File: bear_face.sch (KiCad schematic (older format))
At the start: 275 parts, among them J1 USB_B_Micro, SW1 SW_Push, U1 ATmega32U4-AU, Y1 16MHz

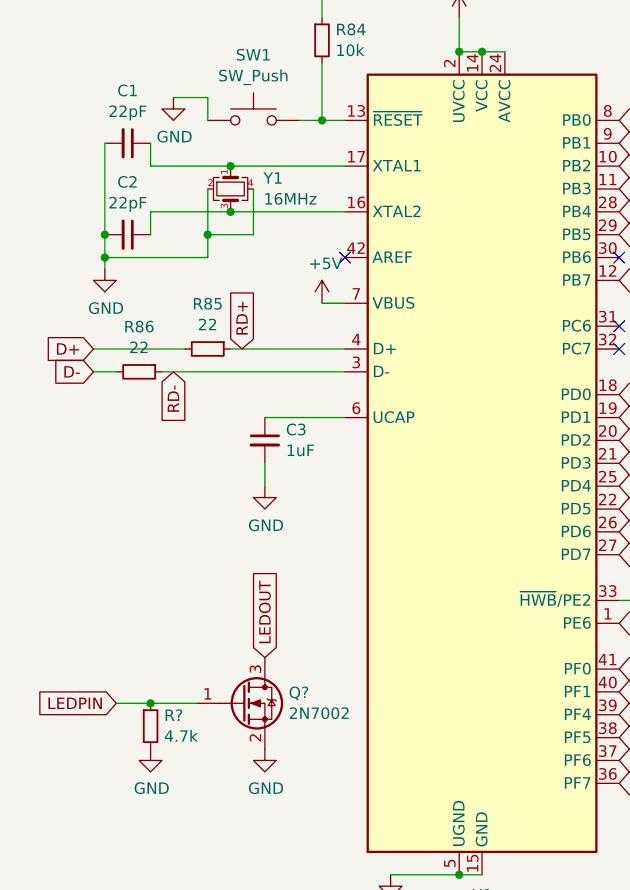
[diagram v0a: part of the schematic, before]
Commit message: Changed MCU components back to SMD
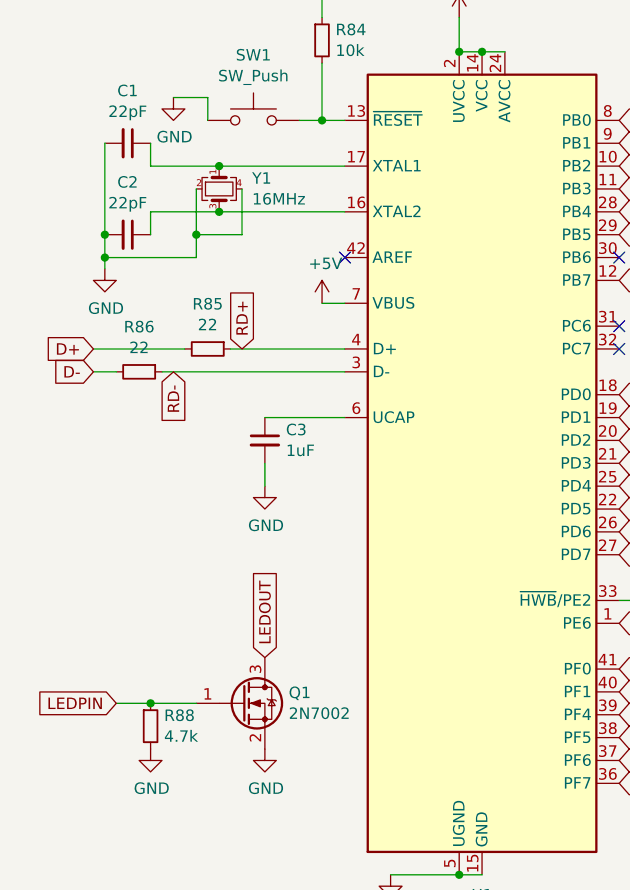
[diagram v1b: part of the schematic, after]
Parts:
- R85, R86: footprint Resistor_SMD:R_0805_2012Metric -> bear_face_parts:Resistor-THT
- R88: renamed from R?; footprint (none) -> bear_face_parts:Resistor-THT
- gave numbers to parts that had none: 1
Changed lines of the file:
@@
 F 0 "R85" V 1004 4800 50  0000 C CNN
 F 1 "22" V 1095 4800 50  0000 C CNN
-F 2 "Resistor_SMD:R_0805_2012Metric" H 1200 4800 50  0001 C CNN
+F 2 "bear_face_parts:Resistor-THT" H 1200 4800 50  0001 C CNN
 F 3 "~" H 1200 4800 50  0001 C CNN
 	1    1200 4800
@@
 F 0 "R86" V 704 4900 50  0000 C CNN
 F 1 "22" V 795 4900 50  0000 C CNN
-F 2 "Resistor_SMD:R_0805_2012Metric" H 900 4900 50  0001 C CNN
+F 2 "bear_face_parts:Resistor-THT" H 900 4900 50  0001 C CNN
 F 3 "~" H 900 4900 50  0001 C CNN
 	1    900  4900
@@
 	750  3900 750  4300
 Connection ~ 750  4300
-Wire Wire Line
-	750  4300 750  4400
 $Comp
 L power:GND #PWR08
@@
 Text GLabel 10950 4950 2    50   Input ~ 0
 ROW5
-Wire Wire Line
-	950  4000 1300 4000
-Wire Wire Line
-	950  4200 1300 4200
-$Comp
-L Device:Crystal_GND24_Small Y1
-U 1 1 5EE4C65A
-P 1300 4100
-F 0 "Y1" V 1254 4244 50  0000 L CNN
-F 1 "16MHz" V 1345 4244 50  0000 L CNN
-F 2 "Crystal:Crystal_SMD_3225-4Pin_3.2x2.5mm" H 1300 4100 50  0001 C CNN
-F 3 "~" H 1300 4100 50  0001 C CNN
-	1    1300 4100
-	0    1    1    0
-$EndComp
-Connection ~ 1300 4000
-Wire Wire Line
-	1300 4000 1800 4000
-Connection ~ 1300 4200
-Wire Wire Line
-	1300 4200 1800 4200
-Wire Wire Line
-	1200 4100 1200 4300
-Wire Wire Line
-	750  4400 1200 4400
-Connection ~ 750  4400
-Wire Wire Line
-	750  4400 750  4450
-Wire Wire Line
-	1400 4100 1400 4300
-Wire Wire Line
-	1400 4300 1200 4300
-Connection ~ 1200 4300
-Wire Wire Line
-	1200 4300 1200 4400
 Text GLabel 800  6350 0    50   Input ~ 0
 LEDPIN
 $Comp
-L Transistor_FET:2N7002 Q?
+L Transistor_FET:2N7002 Q1
 U 1 1 5E2E1EE1
 P 1350 6350
-F 0 "Q?" H 1554 6396 50  0000 L CNN
+F 0 "Q1" H 1554 6396 50  0000 L CNN
 F 1 "2N7002" H 1554 6305 50  0000 L CNN
 F 2 "Package_TO_SOT_SMD:SOT-23" H 1550 6275 50  0001 L CIN
@@
 LEDOUT
 $Comp
-L power:GND #PWR?
+L power:GND #PWR0101
 U 1 1 5E2E9481
 P 1450 6550
-F 0 "#PWR?" H 1450 6300 50  0001 C CNN
+F 0 "#PWR0101" H 1450 6300 50  0001 C CNN
 F 1 "GND" H 1455 6377 50  0000 C CNN
 F 2 "" H 1450 6550 50  0001 C CNN
@@
 	800  6350 950  6350
 $Comp
-L Device:R_Small R?
+L Device:R_Small R88
 U 1 1 5E33D046
 P 950 6450
-F 0 "R?" H 1009 6496 50  0000 L CNN
+F 0 "R88" H 1009 6496 50  0000 L CNN
 F 1 "4.7k" H 1009 6405 50  0000 L CNN
-F 2 "" H 950 6450 50  0001 C CNN
+F 2 "bear_face_parts:Resistor-THT" H 950 6450 50  0001 C CNN
 F 3 "~" H 950 6450 50  0001 C CNN
 	1    950  6450
@@
 	950  6350 1150 6350
 $Comp
-L power:GND #PWR?
+L power:GND #PWR0102
 U 1 1 5E33ECD1
 P 950 6550
-F 0 "#PWR?" H 950 6300 50  0001 C CNN
+F 0 "#PWR0102" H 950 6300 50  0001 C CNN
 F 1 "GND" H 955 6377 50  0000 C CNN
 F 2 "" H 950 6550 50  0001 C CNN
@@
 	1    0    0    -1
 $EndComp
+Wire Wire Line
+	750  4300 750  4400
+Wire Wire Line
+	950  4000 1250 4000
+Wire Wire Line
+	950  4200 1250 4200
+$Comp
+L Device:Crystal_GND24_Small Y1
+U 1 1 5E291FCA
+P 1250 4100
+F 0 "Y1" V 1204 4244 50  0000 L CNN
+F 1 "16MHz" V 1295 4244 50  0000 L CNN
+F 2 "Crystal:Crystal_SMD_3225-4Pin_3.2x2.5mm" H 1250 4100 50  0001 C CNN
+F 3 "~" H 1250 4100 50  0001 C CNN
+	1    1250 4100
+	0    1    1    0
+$EndComp
+Connection ~ 1250 4000
+Wire Wire Line
+	1250 4000 1800 4000
+Connection ~ 1250 4200
+Wire Wire Line
+	1250 4200 1800 4200
+Wire Wire Line
+	1150 4100 1150 4300
+Wire Wire Line
+	1150 4400 750  4400
+Connection ~ 750  4400
+Wire Wire Line
+	750  4400 750  4450
+Wire Wire Line
+	1350 4100 1350 4300
+Wire Wire Line
+	1350 4300 1150 4300
+Connection ~ 1150 4300
+Wire Wire Line
+	1150 4300 1150 4400
 $EndSCHEMATC

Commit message: USB track drawn first
Tracks wiped, footprints for resistors shrunk down, USB tracks drawn first
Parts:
- R1, R10, R11, R12, R13, R14, R15, R16, R17, R18, R19, R2, R20, R21, R22, R23, R24, R25, R26, R27, R28, R29, R3, R30, R31, R32, R33, R34, R35, R36, R37, R38, R39, R4, R40, R41, R42, R43, R44, R45, R46, R47, R48, R49, R5, R50, R51, R52, R53, R54, R55, R56, R57, R58, R59, R6, R60, R61, R62, R63, R64, R65, R66, R67, R68, R69, R7, R70, R71, R72, R73, R74, R75, R76, R77, R78, R79, R8, R80, R81, R82, R83, R85, R86, R88, R9: footprint bear_face_parts:Resistor-THT -> bear_face_parts:Resistor-Compact-1-side

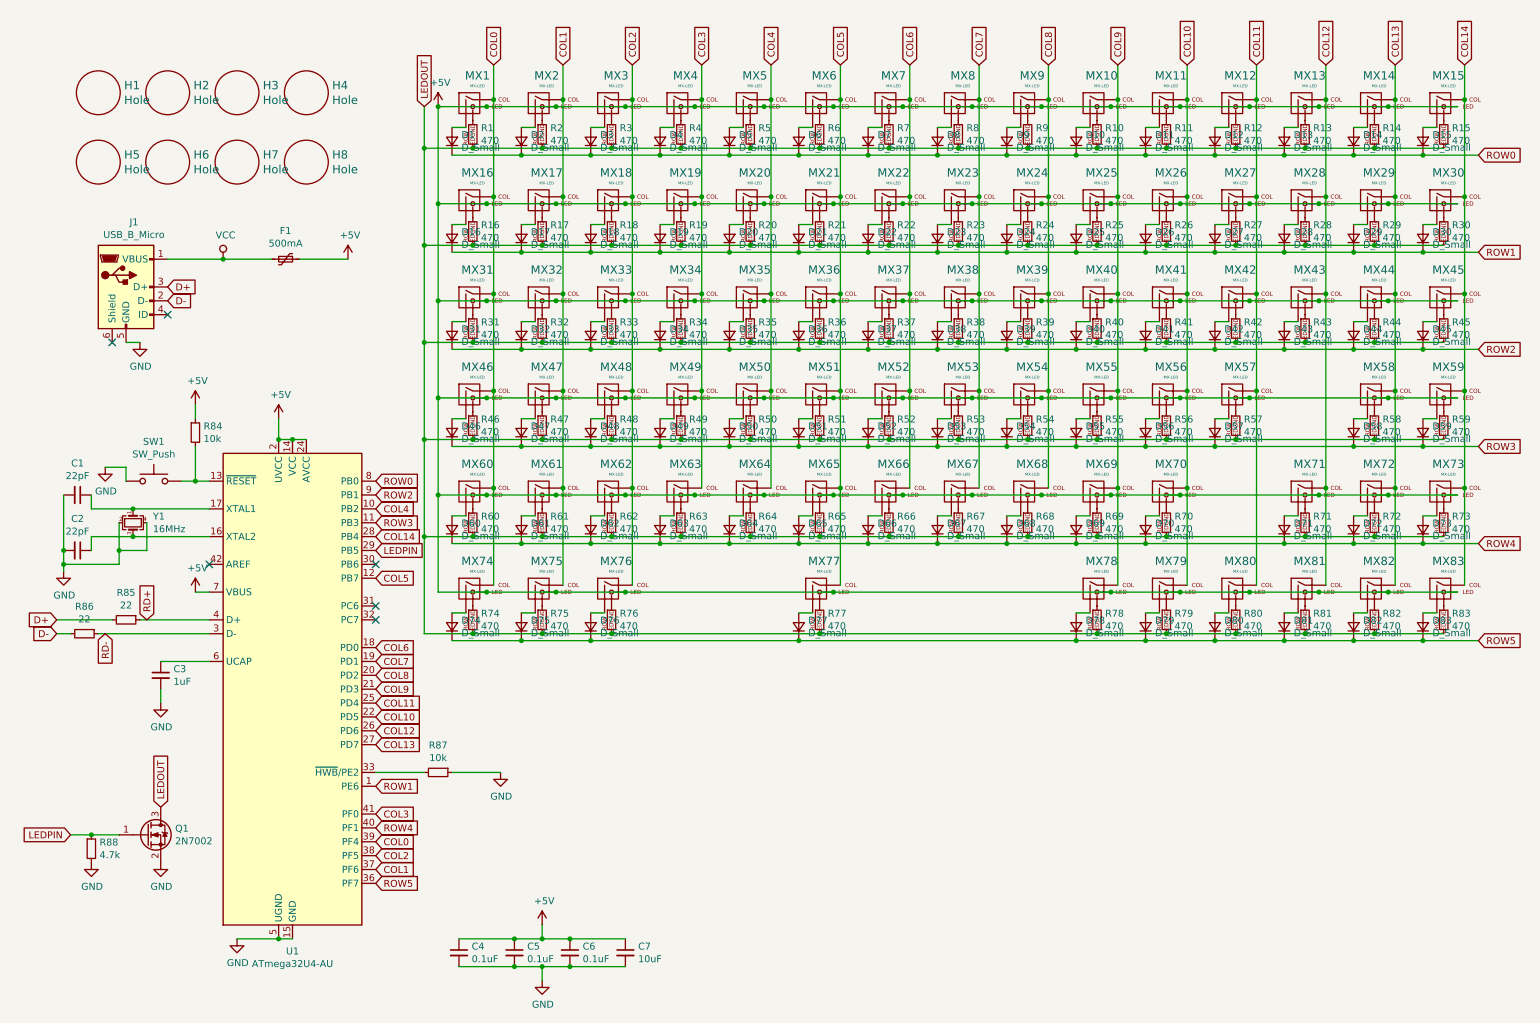
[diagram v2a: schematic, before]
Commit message: Changed footprints, added ESD chip
Dual footprints added
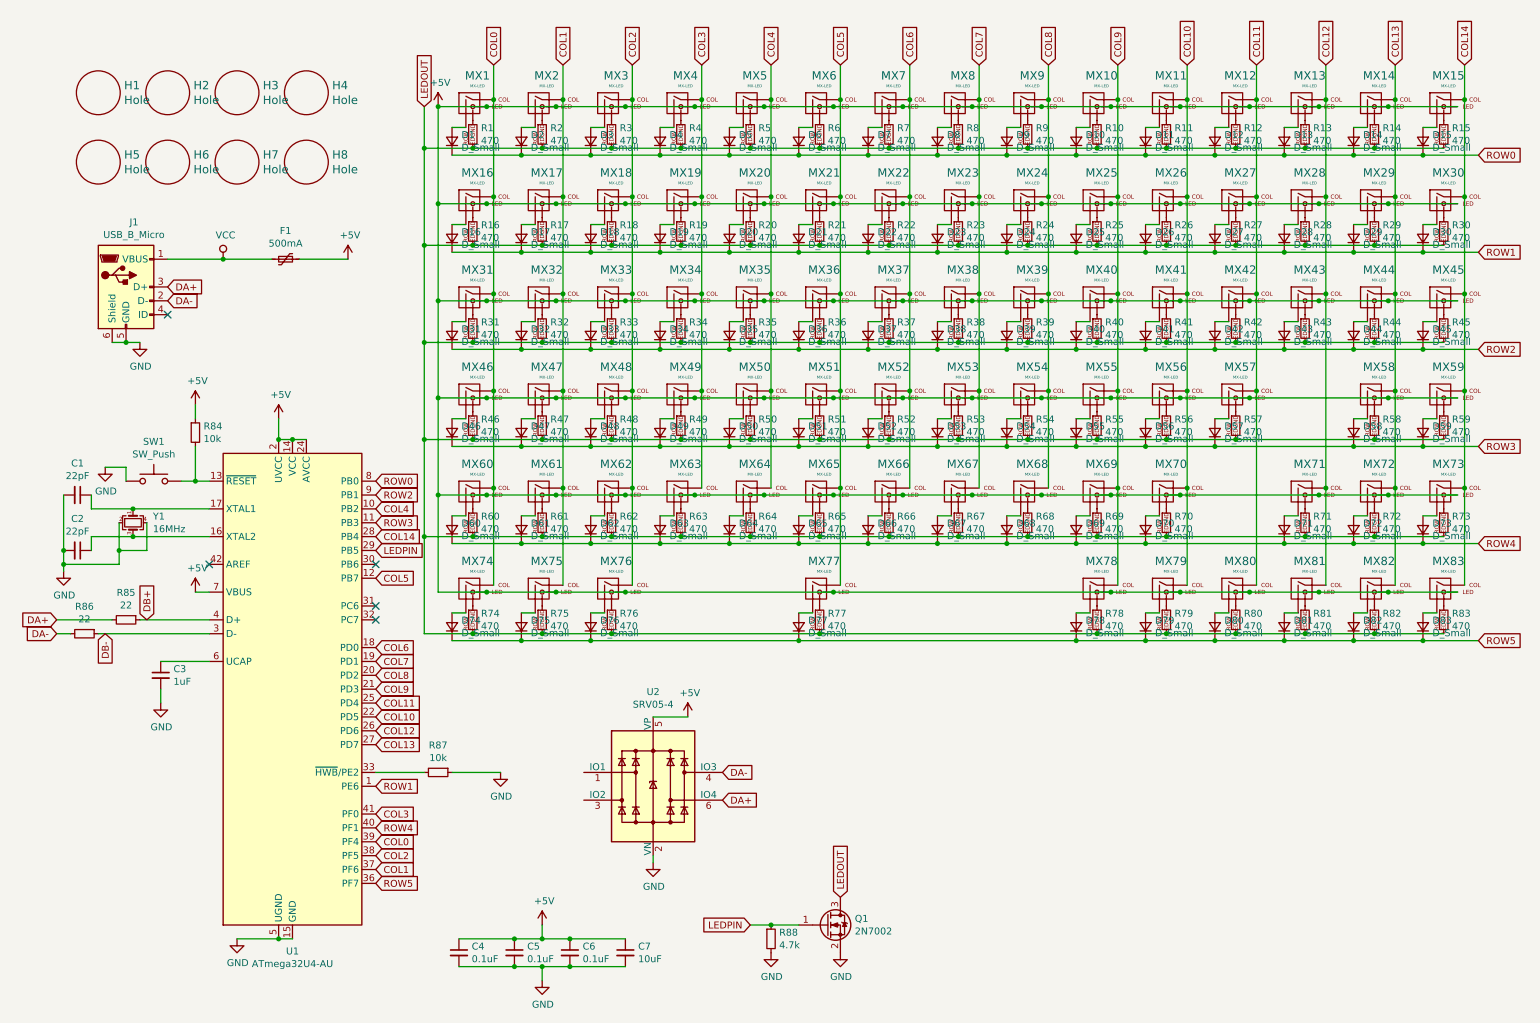
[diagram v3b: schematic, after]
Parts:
- added U2: SRV05-4, Package_TO_SOT_SMD:SOT-23-6, symbol Power_Protection:SRV05-4
- C1, C2, C3, C4, C5, C6, C7: footprint Capacitor_SMD:C_0805_2012Metric -> Capacitor_SMD:C_0805_2012Metric_Pad1.15x1.40mm_HandSolder
- D1, D10, D11, D12, D13, D14, D15, D16, D17, D18, D19, D2, D20, D21, D22, D23, D24, D25, D26, D27, D28, D29, D3, D30, D31, D32, D33, D34, D35, D36, D37, D38, D39, D4, D40, D41, D42, D43, D44, D45, D46, D47, D48, D49, D5, D50, D51, D52, D53, D54, D55, D56, D57, D58, D59, D6, D60, D61, D62, D63, D64, D65, D66, D67, D68, D69, D7, D70, D71, D72, D73, D74, D75, D76, D77, D78, D79, D8, D80, D81, D82, D83, D9: footprint bear_face_parts:Diode-THT -> Keebio-Parts:Diode-dual
- R1, R10, R11, R12, R13, R14, R15, R16, R17, R18, R19, R2, R20, R21, R22, R23, R24, R25, R26, R27, R28, R29, R3, R30, R31, R32, R33, R34, R35, R36, R37, R38, R39, R4, R40, R41, R42, R43, R44, R45, R46, R47, R48, R49, R5, R50, R51, R52, R53, R54, R55, R56, R57, R58, R59, R6, R60, R61, R62, R63, R64, R65, R66, R67, R68, R69, R7, R70, R71, R72, R73, R74, R75, R76, R77, R78, R79, R8, R80, R81, R82, R83, R88, R9: footprint bear_face_parts:Resistor-Compact-1-side -> Keebio-Parts:Resistor-Hybrid
- R84, R87: footprint Resistor_SMD:R_0805_2012Metric -> Resistor_SMD:R_0805_2012Metric_Pad1.15x1.40mm_HandSolder
- R85, R86: footprint bear_face_parts:Resistor-Compact-1-side -> Resistor_SMD:R_0805_2012Metric_Pad1.15x1.40mm_HandSolder
- Y1: footprint Crystal:Crystal_SMD_3225-4Pin_3.2x2.5mm -> Crystal:Crystal_SMD_3225-4Pin_3.2x2.5mm_HandSoldering
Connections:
- net +5V: now also U2.5 (VP)
- net GND: now also J1.6 (Shield), U2.2 (VN)
- net D+ renamed DA+
- net DA+: now also U2.6 (IO4)
- net D- renamed DA-
- net DA-: now also U2.4 (IO3)
- net RD+ renamed DB+
- net RD- renamed DB-
- no-connect marks 6 -> 5
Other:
- moved on the sheet: Q1, R88
